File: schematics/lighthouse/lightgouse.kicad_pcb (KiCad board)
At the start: 2 copper layers, 11 parts, among them P1 3V3, P2 GND, U1 ESP-201, U2 rc522

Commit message: lighthouse schematic update
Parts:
- moved R1 17.8 mm to (132.1, 104.1), turned to 270 degrees
- moved D1 6.48 mm to (125.7, 113.0)
- moved D2 5.24 mm to (129.5, 118.1)
- moved R2 2.54 mm to (129.5, 101.6)
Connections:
- U1 pad 13: Net-(R1-Pad1) -> Net-(U1-Pad13)
- U1 pad 6: Net-(U1-Pad6) -> Net-(R1-Pad1)
- U2 pad 1: Net-(U1-Pad6) -> Net-(U1-Pad13)
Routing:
- net Net-(U1-Pad13): track 0.00 -> 75.3 mm
- net Net-(U1-Pad17): track 33.0 -> 17.8 mm
- net Net-(P1-Pad1): track 72.8 -> 63.2 mm
- net Net-(D1-Pad1): track 73.2 -> 65.3 mm
- net Net-(R2-Pad1): track 2.54 -> 5.08 mm
- net Net-(D1-Pad2): track 6.13 -> 4.34 mm

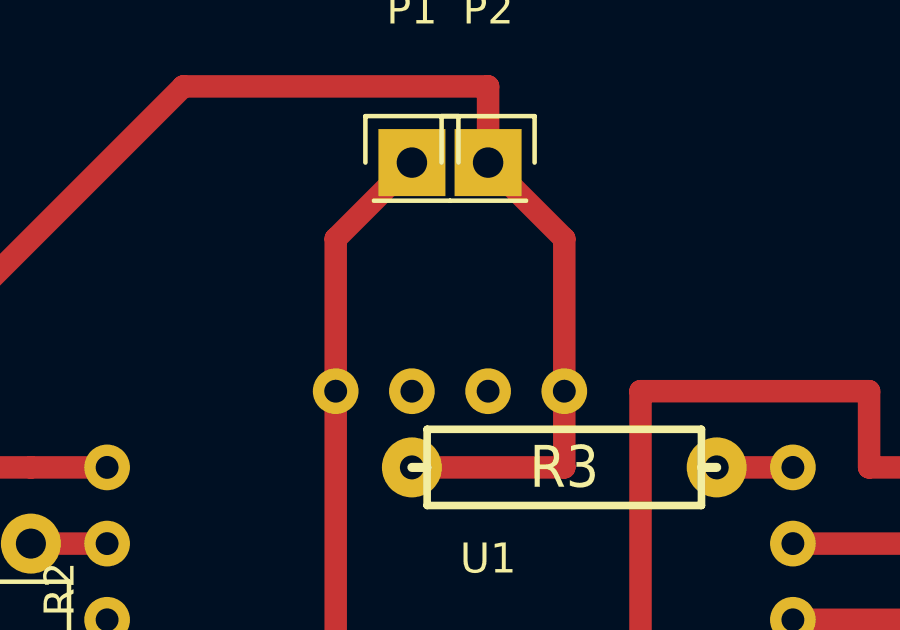
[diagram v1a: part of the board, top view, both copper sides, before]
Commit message: Update schematics for whiskers
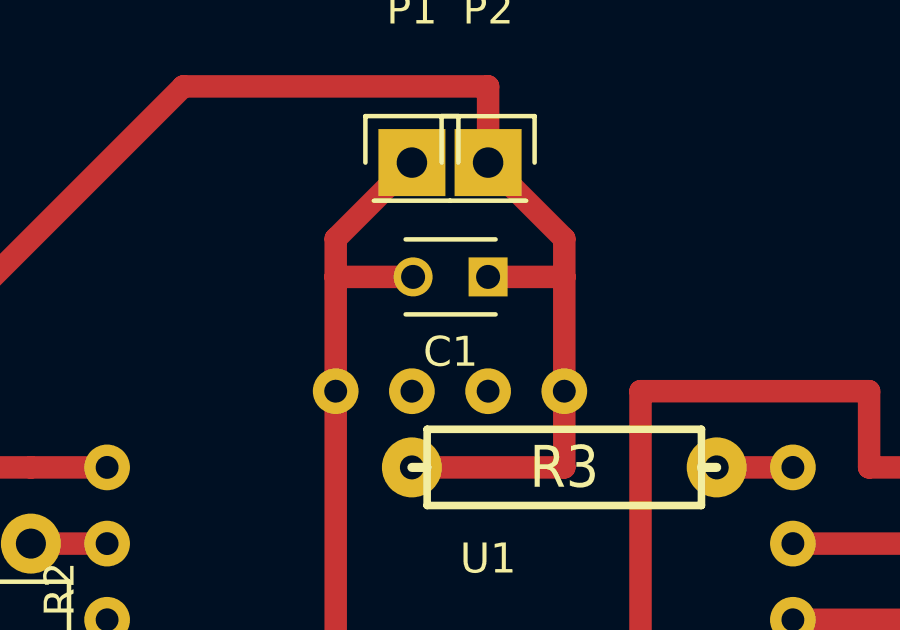
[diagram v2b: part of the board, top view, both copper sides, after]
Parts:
- added C1: C, Capacitors_ThroughHole:C_Disc_D3_P2.5, F.Cu at (147.3, 95.2)
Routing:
- net Net-(C1-Pad2): track 63.2 -> 65.8 mm
- net Net-(C1-Pad1): track 65.3 -> 67.8 mm

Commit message: SCHEMATICS: prepare Lighthouse for production
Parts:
- removed C1: C, Capacitors_ThroughHole:C_Disc_D3_P2.5
- added C2: 100mkF, bugs:capasitor, F.Cu at (116.8, 91.4)
- added C3: 1000mkF, bugs:capasitor, F.Cu at (147.3, 88.9)
- added D3: D_Schottky, Diodes_ThroughHole:Diode_DO-41_SOD81_Horizontal_RM10, F.Cu at (132.1, 86.4)
- added L1: 100mkH, Discret:CP4, F.Cu at (137.2, 91.4)
- added P3: TX, Pin_Headers:Pin_Header_Straight_1x01, F.Cu at (147.3, 96.5)
- added P4: RX, Pin_Headers:Pin_Header_Straight_1x01, F.Cu at (144.8, 96.5)
- added U3: LM2576, TO_SOT_Packages_THT:Pentawatt_Neutral_Straight_Vertical_TO220-5-T05A, F.Cu at (124.5, 88.9)
- moved P2 35.7 mm to (111.8, 88.9)
- moved P1 33.0 mm to (111.8, 91.4)
- moved U2 2.54 mm to (165.1, 106.7)
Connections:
- P1 pad 1: Net-(C1-Pad2) -> Net-(C2-Pad1)
- R4 pad 1: Net-(C1-Pad2) -> Net-(C3-Pad1)
- R5 pad 1: Net-(C1-Pad2) -> Net-(C3-Pad1)
- U1 pad 1: Net-(C1-Pad2) -> Net-(C3-Pad1)
- U2 pad 8: Net-(C1-Pad2) -> Net-(C3-Pad1)
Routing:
- net Net-(C3-Pad1): track 0.00 -> 82.3 mm
- net Net-(C1-Pad2): track 65.8 -> 0.00 mm
- net Net-(C2-Pad2): track 67.8 -> 111.6 mm
- net Net-(U1-Pad18): track 12.7 -> 35.6 mm
- net Net-(C2-Pad1): track 0.00 -> 13.7 mm
- net Net-(D3-Pad1): track 0.00 -> 13.6 mm
- net Net-(U1-Pad13): track 75.3 -> 83.8 mm
- net Net-(P4-Pad1): track 0.00 -> 2.54 mm
- net Net-(P3-Pad1): track 0.00 -> 2.54 mm
- net Net-(U1-Pad25): track 5.08 -> 7.62 mm
- net Net-(U1-Pad24): track 5.08 -> 7.62 mm
- net Net-(U1-Pad23): track 27.9 -> 30.5 mm
- net Net-(U1-Pad17): track 17.8 -> 20.3 mm
